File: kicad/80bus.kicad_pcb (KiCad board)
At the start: 2 copper layers, 145 x 130 mm, 76 parts, among them Q1 VP3203N3-G, SW1 SW_SPDT, T1 10uF, T2 10uF, U1 4049, U2 TL497_Fixed, U3 LM78L12_TO92, U4 4040, U5 LMC7660

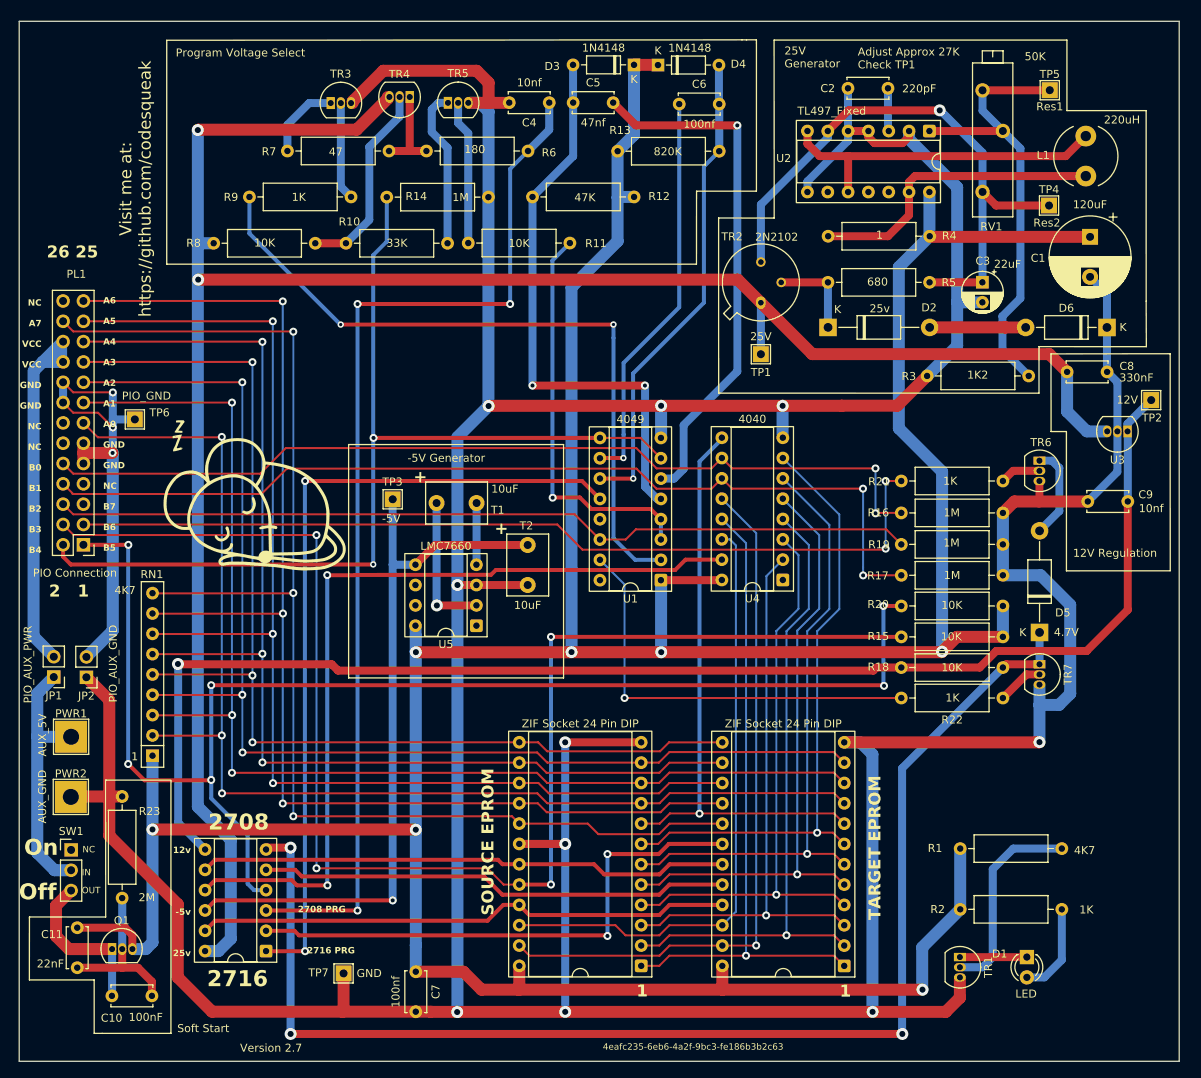
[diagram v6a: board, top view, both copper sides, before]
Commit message: Update footprints
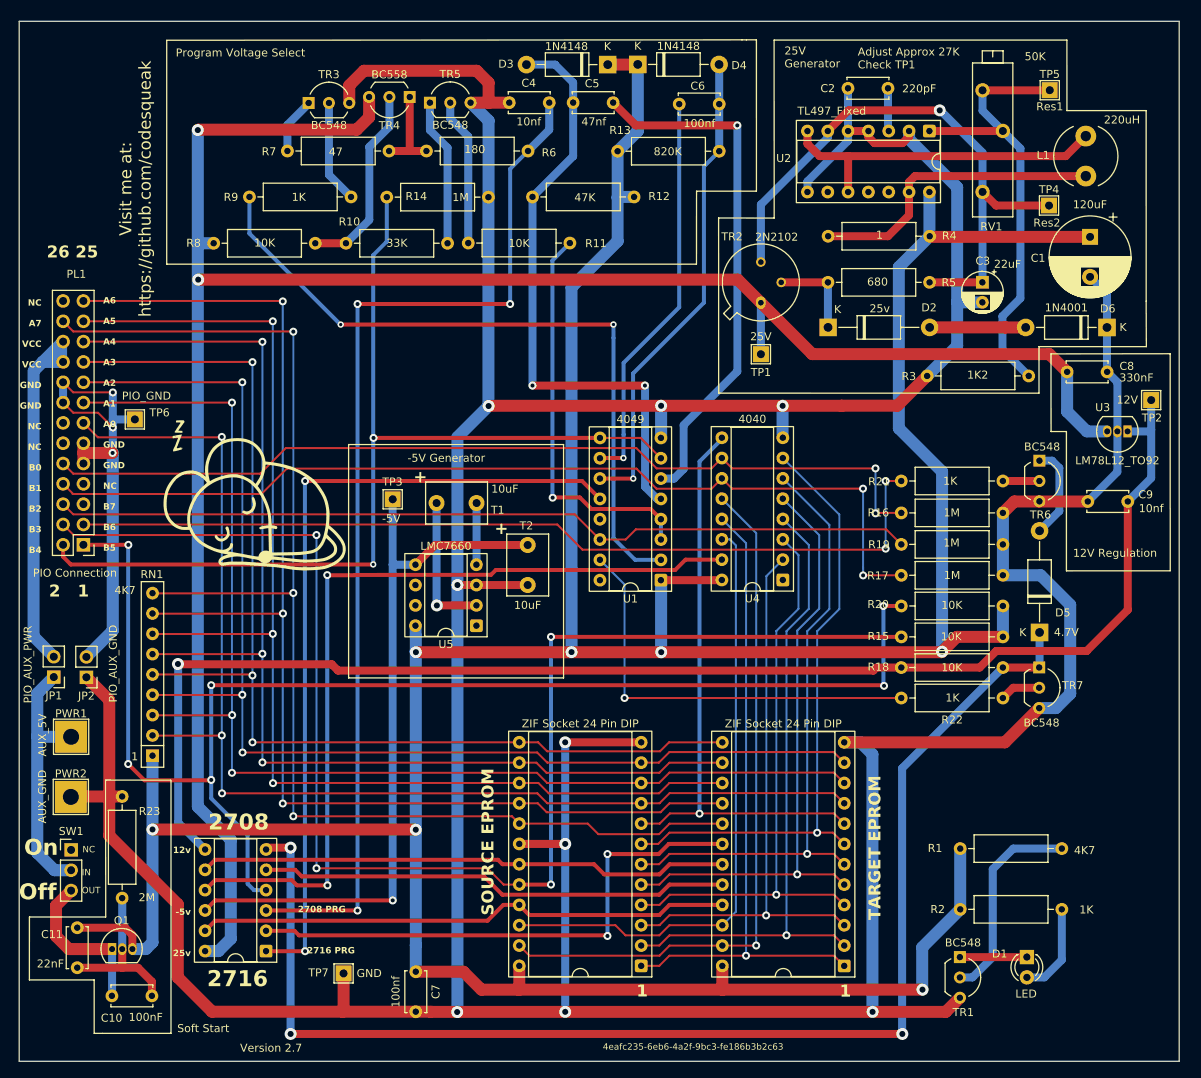
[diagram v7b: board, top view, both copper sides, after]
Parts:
- D3, D4: footprint Diode_THT:D_DO-35_SOD27_P7.62mm_Horizontal -> Diode_THT:D_DO-41_SOD81_P10.16mm_Horizontal
- TR1, TR3, TR4, TR5, TR6, TR7: footprint Package_TO_SOT_THT:TO-92_Inline -> Package_TO_SOT_THT:TO-92_Inline_Wide
- moved D3 3.28 mm to (203.6, 80.4)
- moved TR3 2.76 mm to (166.2, 85.2)
- moved D4 2.53 mm to (207.3, 80.4)
- moved TR5 2.25 mm to (181.3, 85.2)
- moved TR7 0.40 mm to (257.5, 155.8)
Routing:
- net GND: track 630.3 -> 621.1 mm, vias 10 -> 9
- net Net-(D3-A): track 71.5 -> 76.1 mm
- net GENERATED 12V: track 173.7 -> 176.7 mm
- net Net-(TR3-C): track 9.81 -> 7.12 mm
- net Net-(TR5-C): track 19.9 -> 18.5 mm
- net SWITCHED 5V: track 458.6 -> 459.6 mm
- net GENERATED 25V: track 264.8 -> 263.9 mm
- net Net-(TR7-B): track 5.79 -> 5.07 mm
- net Net-(TR3-B): track 12.3 -> 12.9 mm
- net Net-(TR4-B): track 24.9 -> 24.4 mm
- net Net-(TR6-B): track 5.09 -> 4.57 mm
- net Net-(TR1-B): track 25.3 -> 25.9 mm
